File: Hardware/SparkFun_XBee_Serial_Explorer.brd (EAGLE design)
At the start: 48.3 x 57.1 mm, 42 parts, among them J1 POWER_JACKPTH, Q1 MBT2222, U1 MAX232SOIC16, U2 XBEE-1B3, U3 LM317, X1 RS232

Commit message: Board rev in progress
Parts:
- LOGO2: value SFE_LOGO_NAME_FLAME.1_INCH -> SFE_LOGO_NAME_FLAME.2_INCH; device SparkFun-Aesthetics:SFE_LOGO_NAME_FLAME_.1 -> SparkFun-Aesthetics:SFE_LOGO_NAME_FLAME_.2
- moved LOGO2 24.2 mm to (24.1, 31.8), flipped to the bottom, turned to 270 degrees
- moved LED4 22.9 mm to (45.7, 35.6)
- moved LED2 21.6 mm to (45.7, 41.9)
- moved LED3 20.3 mm to (45.7, 48.3)
- moved LOGO1 6.84 mm to (29.2, 19.1)
- moved J1 6.84 mm to (-2.54, 47.0), turned to 270 degrees
- moved R11 3.81 mm to (26.7, 53.3)
- moved C7 2.84 mm to (15.2, 45.7)
- moved LED1 2.54 mm to (30.5, 53.3)
- moved S1 2.54 mm to (20.3, 53.3)
- moved S3 1.27 mm to (34.3, 45.7)
- moved JP2 1.27 mm to (15.2, 35.6)
- moved Q1 1.27 mm to (16.5, 14.0)
- moved R7 1.27 mm to (14.0, 14.0)
- moved C8 1.27 mm to (20.3, 43.2)
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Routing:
- net N$2: track 7.24 -> 27.9 mm
- net DIN: track 59.3 -> 78.2 mm
- net N$1: track 5.46 -> 23.8 mm
- net DOUT: track 46.7 -> 64.4 mm
- net N$4: track 5.46 -> 22.5 mm
- net RAW: track 73.4 -> 80.1 mm
- net N$11: track 8.08 -> 13.3 mm
- net DTR: track 35.7 -> 39.7 mm
- net N$38: track 3.48 -> 6.39 mm
- net CTS: track 28.8 -> 30.8 mm
- net RSSI: track 34.0 -> 36.0 mm
- net N$15: track 13.1 -> 11.2 mm
- net N$10: track 5.64 -> 7.19 mm
- net RESET: track 19.6 -> 21.1 mm
- net N$12: track 1.70 -> 3.18 mm
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
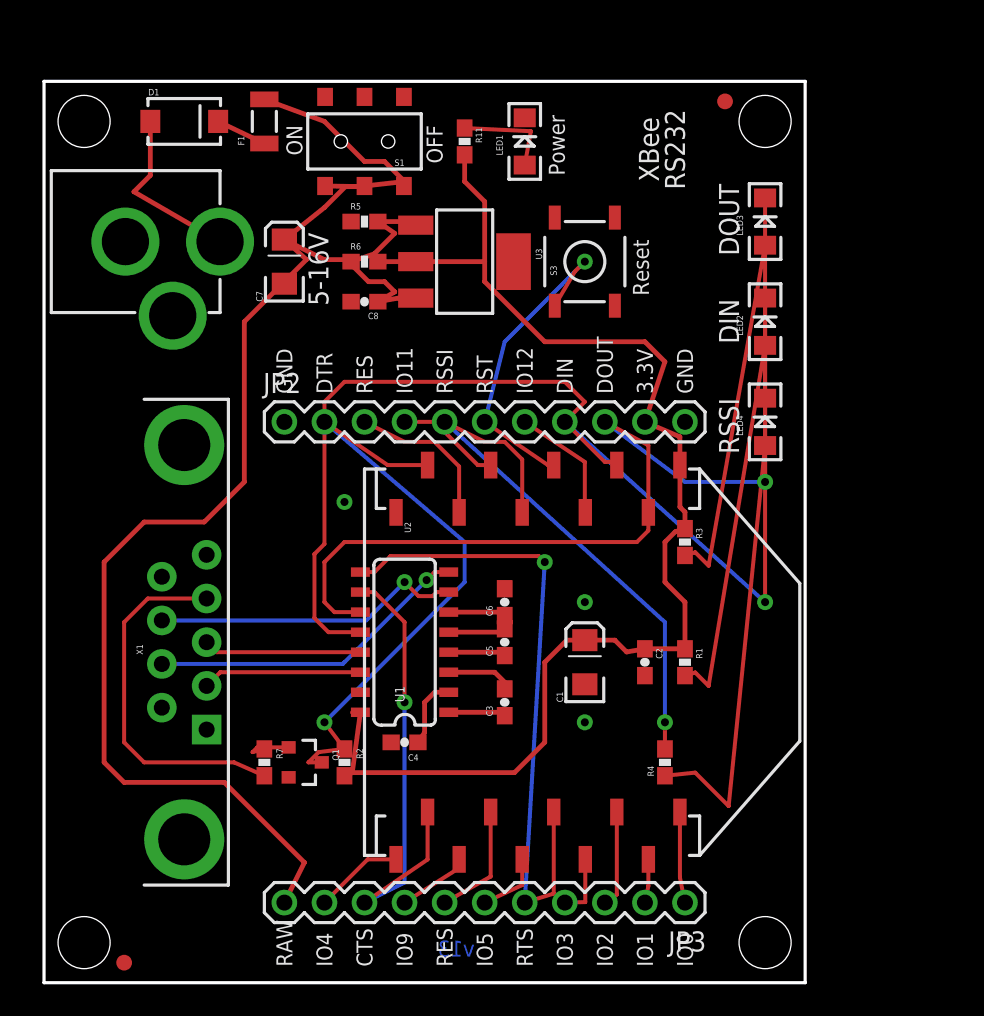
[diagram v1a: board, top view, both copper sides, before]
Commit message: Rerouting, updating parts to PTH, add dimensions, etc.
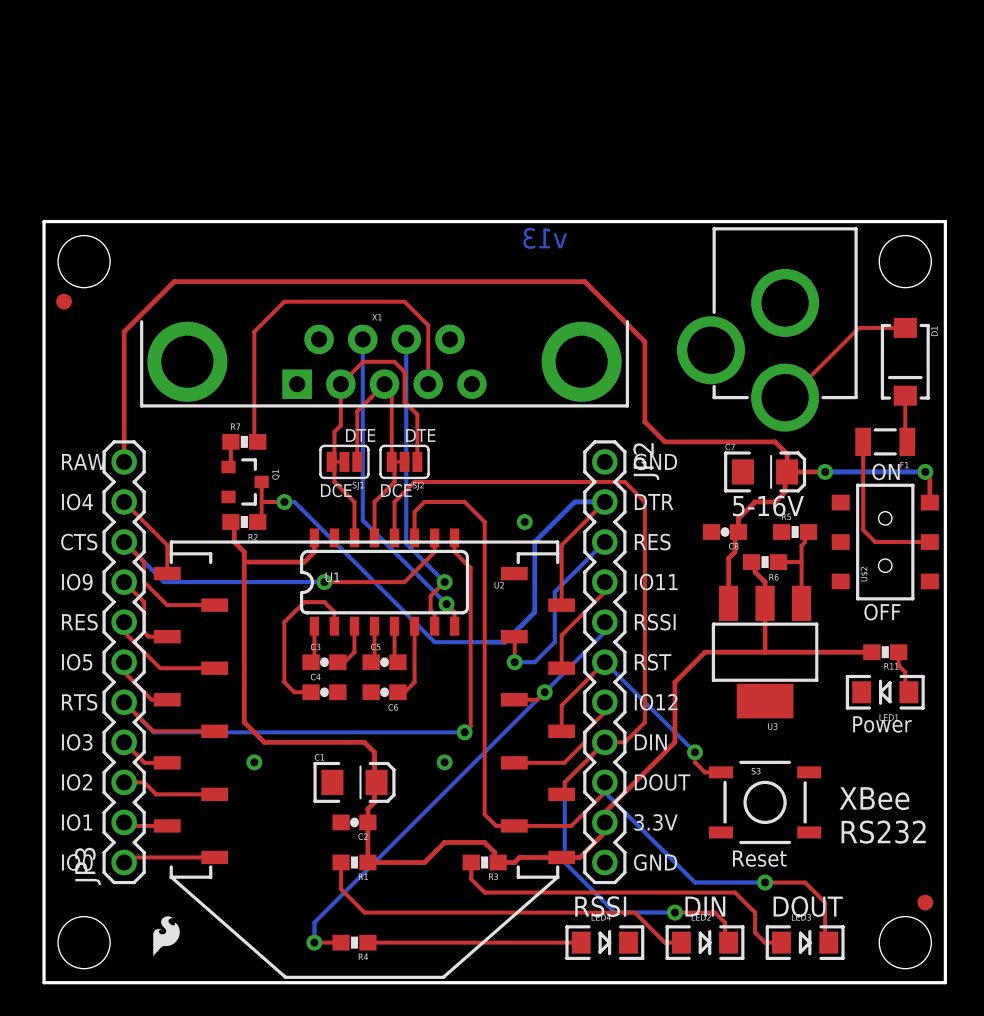
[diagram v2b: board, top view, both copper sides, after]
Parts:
- removed S1: Power, SparkFun:AYZ0202
- added LOGO3: SFE_LOGO_FLAME.1_INCH, SparkFun-Aesthetics:SFE_LOGO_FLAME_.1
- added SJ1, SJ2: JUMPER-PAD-3-2OF3_NC_BY_TRACE_SMALL, SparkFun-Passives:PAD-JUMPER-3-2OF3_NC_BY_TRACE_YES_SILK_FULL_BOX
- added U$2: AYZ0202, SparkFun-Electromechanical:AYZ0202
- F1: device SparkFun:PTC-1206 -> SparkFun-PowerIC:PTC-1206
- U$10, U$11, U$5, U$9: device SparkFun:STAND-OFF -> SparkFun-Electromechanical:STAND-OFF
- U$16, U$7: device SparkFun:FIDUCIAL-1X2 -> SparkFun-Aesthetics:FIDUCIAL-1X2
- moved U$10 52.8 mm to (54.6, 45.7), turned to 270 degrees
- moved U$9 52.8 mm to (54.6, 2.54), turned to 270 degrees
- moved U$16 52.4 mm to (55.9, 5.08), turned to 270 degrees
- moved J1 49.7 mm to (47.0, 50.8), turned to 180 degrees
- moved D1 48.2 mm to (54.6, 39.4), turned to 270 degrees
- moved LED3 45.8 mm to (48.3, 2.54), turned to 0 degrees
- moved F1 44.3 mm to (53.3, 34.3), turned to 180 degrees
- moved U$11 43.2 mm to (2.54, 45.7), turned to 270 degrees
- moved U$5 43.2 mm to (2.54, 2.54), turned to 270 degrees
- moved U$7 42.1 mm to (1.27, 43.2), turned to 270 degrees
- moved R11 42.0 mm to (53.3, 21.0), turned to 180 degrees
- moved LED1 41.7 mm to (53.3, 18.4), turned to 180 degrees
- moved LED2 39.6 mm to (41.9, 2.54), turned to 0 degrees
- moved S3 36.1 mm to (45.7, 11.4), turned to 0 degrees
- moved JP3 35.7 mm to (5.08, 7.62), turned to 90 degrees
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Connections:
- new net N$13: SJ2.2, U1.13
- new net N$14: SJ1.2, U1.14
- net N$11: now also U$2.5; no longer S1.2
- net RAW: now also U$2.6; no longer S1.3
- net RS232-RX: now also SJ1.1, SJ2.3; no longer U1.13
- net RS232-TX: now also SJ1.3, SJ2.1; no longer U1.14
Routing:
- net DIN: track 78.2 -> 63.3 mm
- net N$2: track 27.9 -> 13.5 mm
- net DOUT: track 64.4 -> 55.0 mm
- net N$9: track 4.46 -> 10.6 mm
- net RS232-TX: track 10.1 -> 16.1 mm
- net N$13: track 0.00 -> 5.35 mm
- net N$14: track 0.00 -> 5.35 mm
- net RESET: track 21.1 -> 16.1 mm
- net RSSI: track 36.0 -> 31.8 mm, vias 1 -> 2
- net N$38: track 6.39 -> 2.81 mm
- net N$11: track 13.3 -> 10.1 mm
- net RES1: track 9.86 -> 12.4 mm, vias 0 -> 1
- net DTR: track 39.7 -> 42.0 mm
- net N$15: track 11.2 -> 9.45 mm
- net RAW: track 80.1 -> 81.7 mm, vias 0 -> 2
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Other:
- board size 48.3 x 57.1 mm -> 57.1 x 48.3 mm
- board text added: "DCE"
- board text added: "DTE"
- board text added: "XBee RS232"
- board text removed: "RS232"
- board text removed: "XBee"

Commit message: Updating board and schematic to address GitHub issues
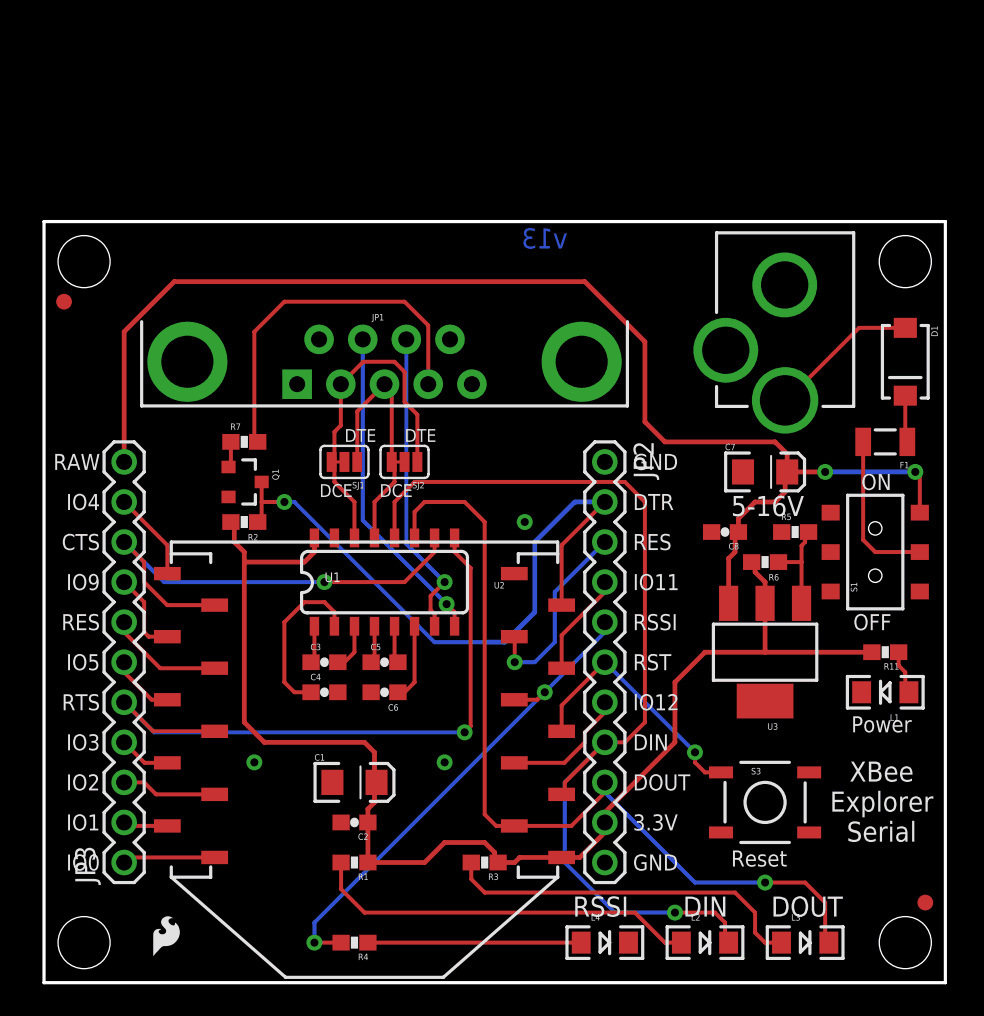
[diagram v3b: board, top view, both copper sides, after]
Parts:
- removed J1: POWER_JACKPTH, SparkFun-Connectors:POWER_JACK_PTH
- removed U$2: AYZ0202, SparkFun-Electromechanical:AYZ0202
- added JP4: POWER_JACKPTH_LOCK, SparkFun-Connectors:POWER_JACK_PTH_LOCK
- added S1: AYZ0202, SparkFun-Electromechanical:AYZ0202
- renumbered LED1 to L1, LED2 to L2, LED3 to L3, LED4 to L4, X1 to JP1
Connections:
- net GND: now also JP4.GND, JP4.GNDBREAK, S3.4; no longer J1.GND, J1.GNDBREAK
- net N$11: now also S1.5; no longer U$2.5
- net N$15: now also JP4.PWR; no longer J1.PWR
- net RAW: now also S1.6; no longer U$2.6
- net RESET: now also S3.2
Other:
- board text added: "XBee Explorer Serial"
- board text removed: "XBee RS232"

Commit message: Fixes for QC checklist
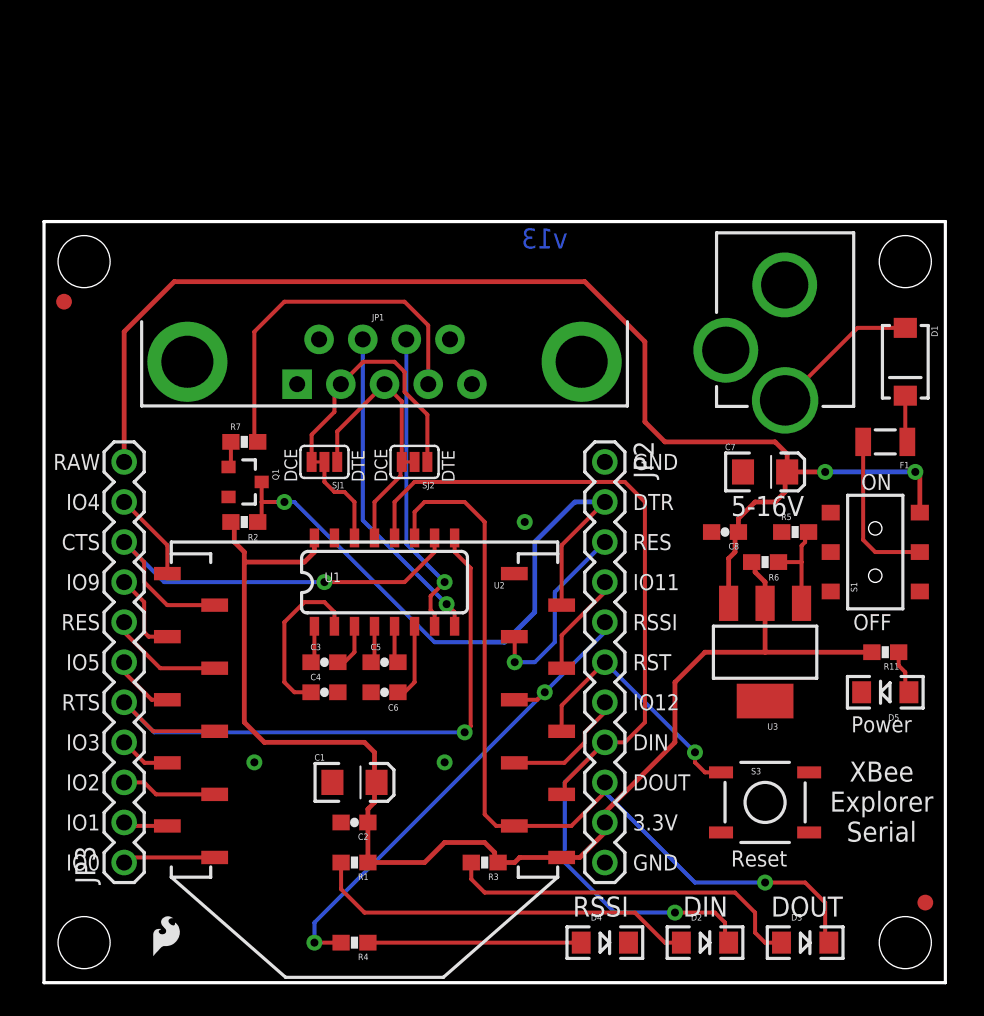
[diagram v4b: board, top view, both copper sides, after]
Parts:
- U3: value LM317 -> LM117; device SparkFun:SOT223 -> SparkFun-PowerIC:SOT223
- moved SJ1 1.27 mm to (17.8, 33.0)
- moved SJ2 0.64 mm to (23.5, 33.0)
- renumbered L1 to D5, L2 to D2, L3 to D3, L4 to D4
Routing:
- net RS232-TX: track 16.1 -> 16.9 mm
- net RS232-RX: track 10.8 -> 11.6 mm
- net N$14: track 5.35 -> 5.98 mm
